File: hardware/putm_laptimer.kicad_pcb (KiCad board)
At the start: 4 copper layers, 93 x 75 mm, 50 parts, among them J1 Conn_01x22, J10 Conn_01x07, J11 Conn_01x07, J12 Conn_01x09, J13 Conn_01x01, J14 Conn_01x01, J15 Conn_01x01, J16 Conn_01x01, J2 Conn_01x22, J3 Conn_01x22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

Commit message: Fixed trace routing
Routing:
- net Net-(D2-A): track 18.5 -> 19.7 mm
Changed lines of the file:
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@@
+	)
+	(segment
+		(start 153.775 99.725)
+		(end 153.5 100)
+		(width 0.2)
+		(layer "F.Cu")
+		(net 19)
+	)
+	(segment
+		(start 153.5 100)
+		(end 153.5 101)
+		(width 0.2)
+		(layer "F.Cu")
+		(net 19)
+	)
+	(segment
+		(start 153.175 101.325)
+		(end 152.5 101.325)
+		(width 0.2)
+		(layer "F.Cu")
+		(net 19)
+	)
+	(segment
+		(start 153.5 101)
+		(end 153.175 101.325)
+		(width 0.2)
+		(layer "F.Cu")
+		(net 19)
 	)
 	(segment
@@
 	)
 	(segment
-		(start 153.775 99.725)
-		(end 153.5 100)
-		(width 0.2)
-		(layer "F.Cu")
-		(net 19)
-	)
-	(segment
-		(start 153.5 100)
-		(end 153.5 101)
-		(width 0.2)
-		(layer "F.Cu")
-		(net 19)
-	)
-	(segment
-		(start 153.175 101.325)
-		(end 152.5 101.325)
-		(width 0.2)
-		(layer "F.Cu")
-		(net 19)
-	)
-	(segment
-		(start 153.5 101)
-		(end 153.175 101.325)
+		(start 152.675 103)
+		(end 152.675 101.5)
 		(width 0.2)
 		(layer "F.Cu")
@@
 		(start 157.545 97.11)
 		(end 161.355 97.11)
-		(width 0.2)
-		(layer "F.Cu")
-		(net 19)
-	)
-	(segment
-		(start 152.675 103)
-		(end 152.675 101.5)
 		(width 0.2)
 		(layer "F.Cu")
@@
 	)
 	(segment
+		(start 190 109)
+		(end 190 107)
+		(width 0.8)
+		(layer "F.Cu")
+		(net 66)
+	)
+	(segment
 		(start 190 114)
 		(end 190 109)
@@
 	)
 	(segment
-		(start 198.5 100.5)
+		(start 190 107)
+		(end 196.5 100.5)
+		(width 0.8)
+		(layer "F.Cu")
+		(net 66)
+	)
+	(segment
+		(start 196.5 100.5)
 		(end 200 100.5)
 		(width 0.8)
 		(layer "F.Cu")
-		(net 66)
-	)
-	(segment
-		(start 190 109)
-		(end 198.5 100.5)
-		(width 0.8)
-		(layer "F.Cu")

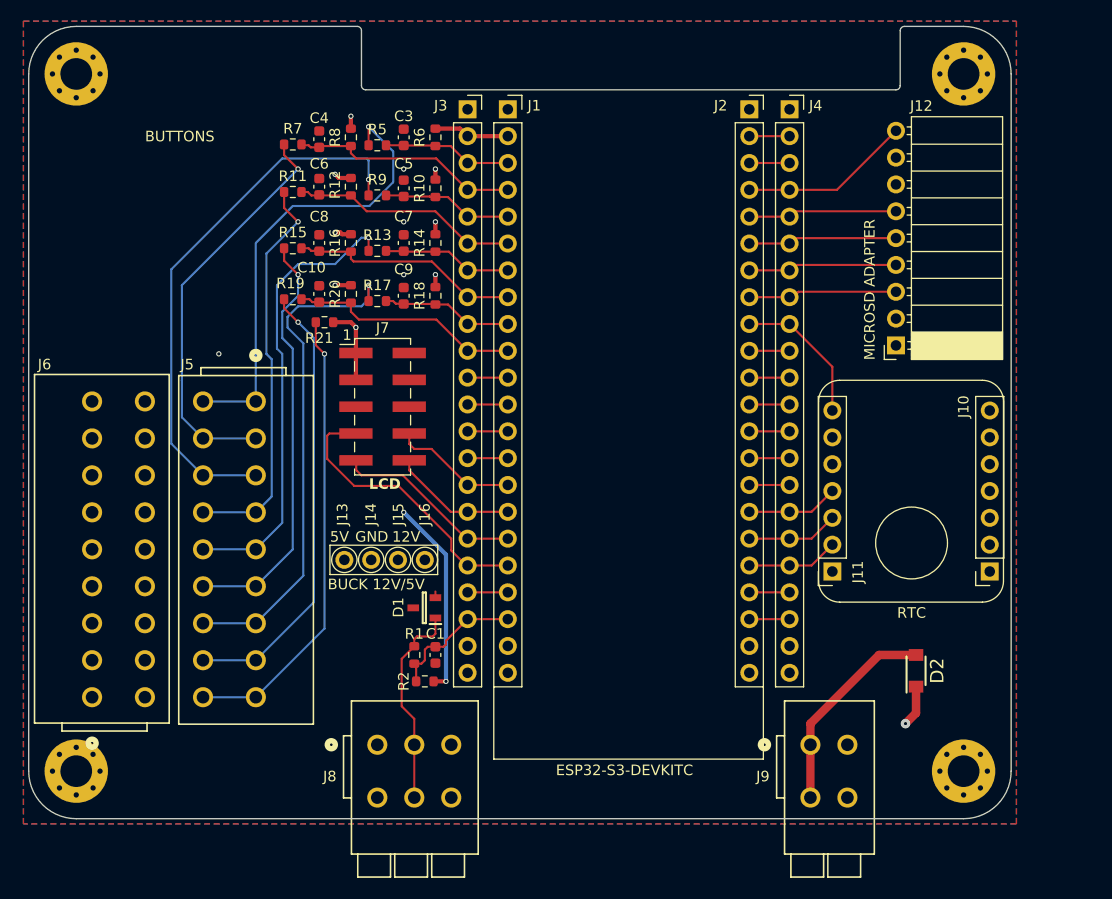
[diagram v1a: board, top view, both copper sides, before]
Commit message: Fixed wago connector place, resized board
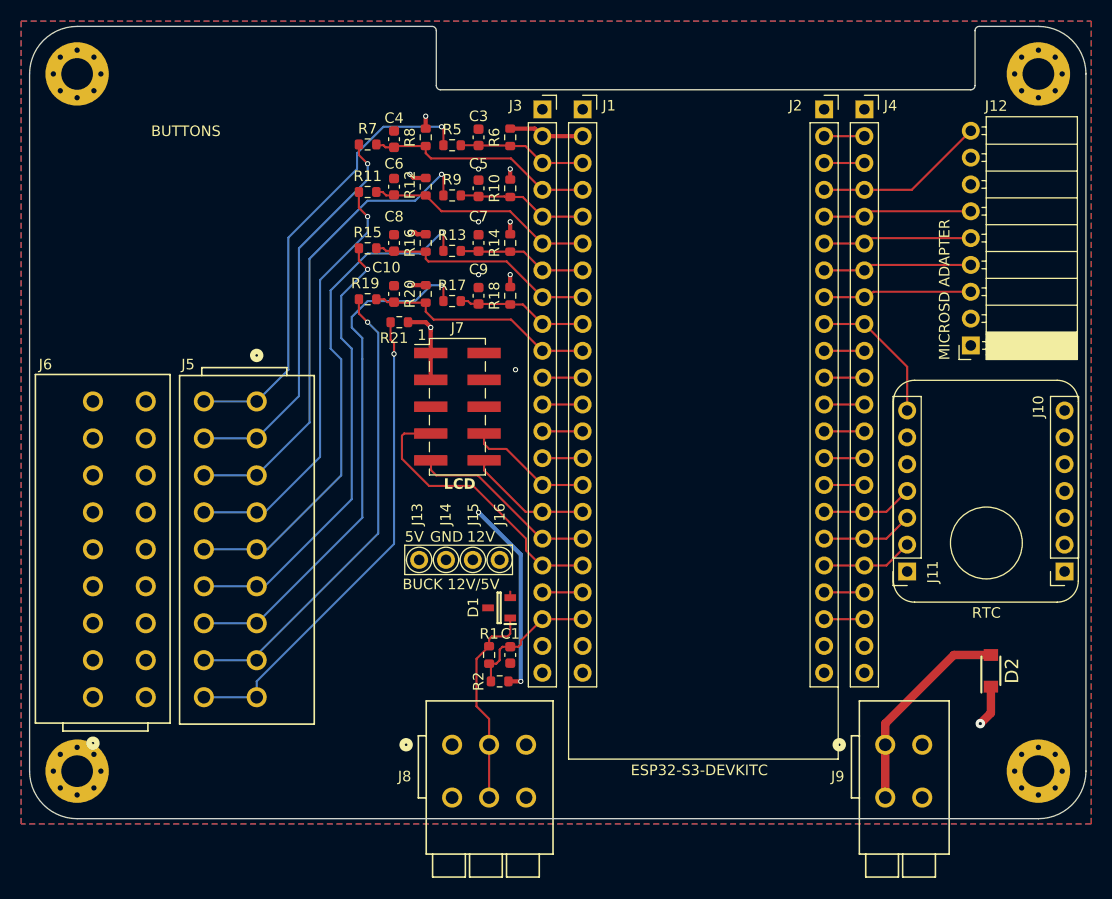
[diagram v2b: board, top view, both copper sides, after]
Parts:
- moved C1 7.08 mm to (161.6, 100.5)
- moved C10 7.08 mm to (150.6, 66.3)
- moved C3 7.08 mm to (158.6, 51.5)
- moved C4 7.08 mm to (150.6, 51.7)
- moved C5 7.08 mm to (158.6, 56.3)
- moved C6 7.08 mm to (150.6, 56.2)
- moved C7 7.08 mm to (158.6, 61.5)
- moved C8 7.08 mm to (150.6, 61.5)
- moved C9 7.08 mm to (158.6, 66.5)
- moved D1 7.08 mm to (160.5, 96.0)
- moved D2 7.08 mm to (207.1, 102.0)
- moved J1 7.08 mm to (168.4, 48.9)
- moved J10 7.08 mm to (214.1, 92.6)
- moved J11 7.08 mm to (199.2, 92.6)
- moved J12 7.08 mm to (205.2, 71.2)
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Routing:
- net /WIFI_BTN: track 52.2 -> 45.5 mm
- net /OC_BTN: track 43.0 -> 48.4 mm
- net /DRIVER_BTN: track 40.0 -> 43.0 mm
- net /DOO_BTN: track 37.9 -> 40.5 mm
- net /PWR_LED: track 43.5 -> 46.0 mm
- net /ADD1_BTN: track 47.7 -> 49.9 mm
- net /ADD2_BTN: track 42.6 -> 44.7 mm
- net /STOP_BTN: track 38.8 -> 37.5 mm
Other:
- board size 93 x 75 mm -> 100 x 75 mm

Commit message: Changed lcd connector model
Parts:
- J7: footprint Connector_PinHeader_2.54mm:PinHeader_2x05_P2.54mm_Vertical_SMD -> Connector_PinHeader_2.54mm:PinHeader_2x05_P2.54mm_Vertical
- moved J7 3.20 mm to (155.7, 73.9)
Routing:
- net +3V3: track 42.7 -> 51.7 mm, vias 10 -> 9
- net /IO12_LCD_DC: track 26.9 -> 21.8 mm
- net /IO11_LCD_SPI_CLK: track 18.0 -> 15.0 mm
- net /IO9_LCD_SPI_MOSI: track 12.2 -> 11.4 mm
- net /IO10_LCD_SPI_CS: track 11.9 -> 11.4 mm
- net GND: vias 4 -> 3

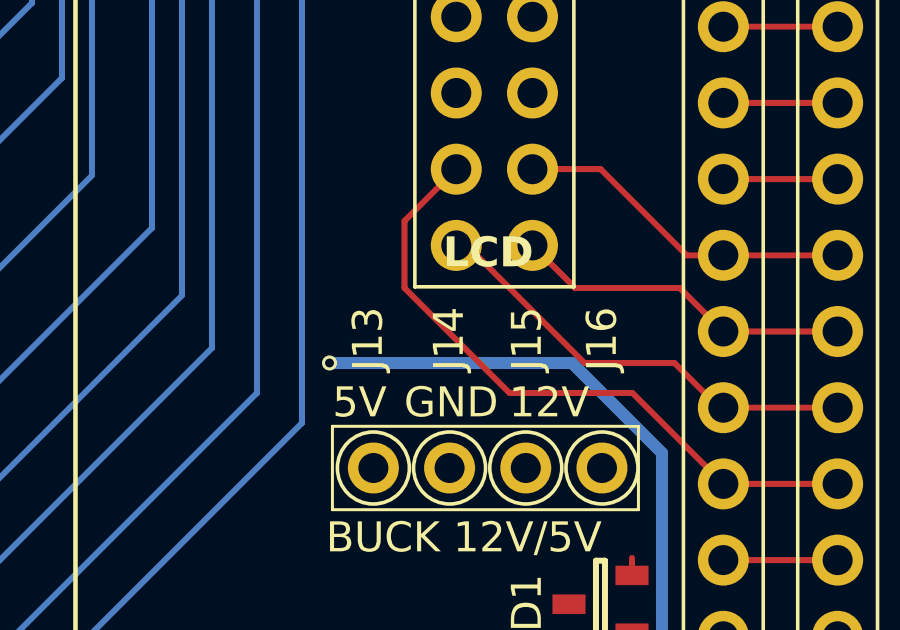
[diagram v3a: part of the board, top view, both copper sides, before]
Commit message: Changed pull up ressistor trace
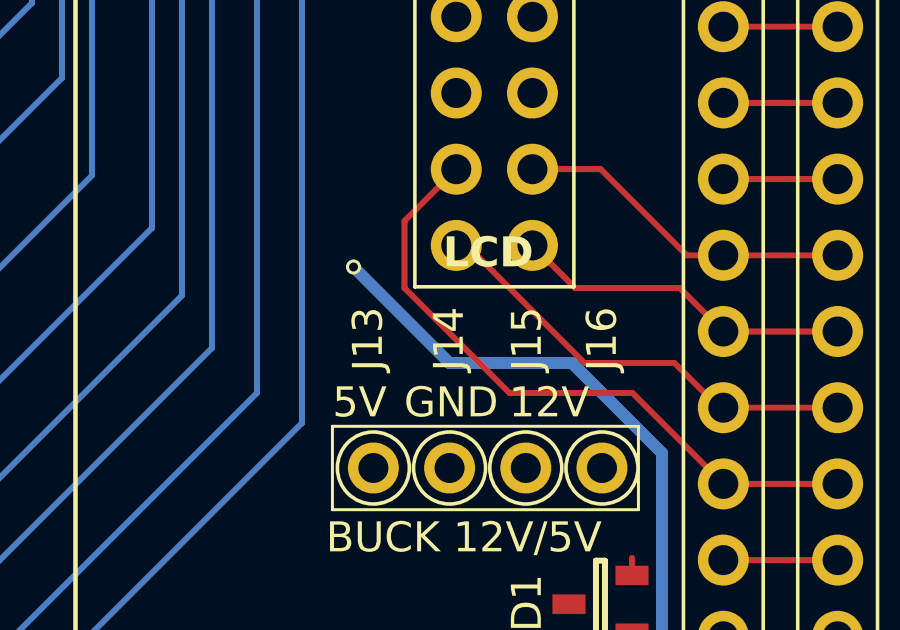
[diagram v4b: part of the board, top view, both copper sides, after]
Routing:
- net +3V3: track 51.7 -> 52.3 mm
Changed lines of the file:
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@@
 	)
 	(via
-		(at 151.5 88)
+		(at 152.3 84.8)
 		(size 0.5)
 		(drill 0.3)
@@
 	)
 	(segment
-		(start 159.581981 88)
-		(end 162.581981 91)
+		(start 155.5 88)
+		(end 159.581981 88)
 		(width 0.4)
 		(layer "B.Cu")
@@
 	)
 	(segment
-		(start 151.5 88)
-		(end 159.581981 88)
+		(start 159.581981 88)
+		(end 162.581981 91)
 		(width 0.4)
 		(layer "B.Cu")
@@
 		(width 0.4)
 		(layer "B.Cu")
+		(net 13)
+	)
+	(segment
+		(start 152.3 84.8)
+		(end 155.5 88)
+		(width 0.4)
+		(layer "B.Cu")
